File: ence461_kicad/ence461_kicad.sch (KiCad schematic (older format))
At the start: 54 parts, among them U1 LMV324, U2 LMV324, U3 LMV324, U4 74HC3G14DP, U5 LMV321, U6 NCV7344D13R2GOSCT-ND, U7 TPS717DRV-WSON, U8 TPS71433DRVR

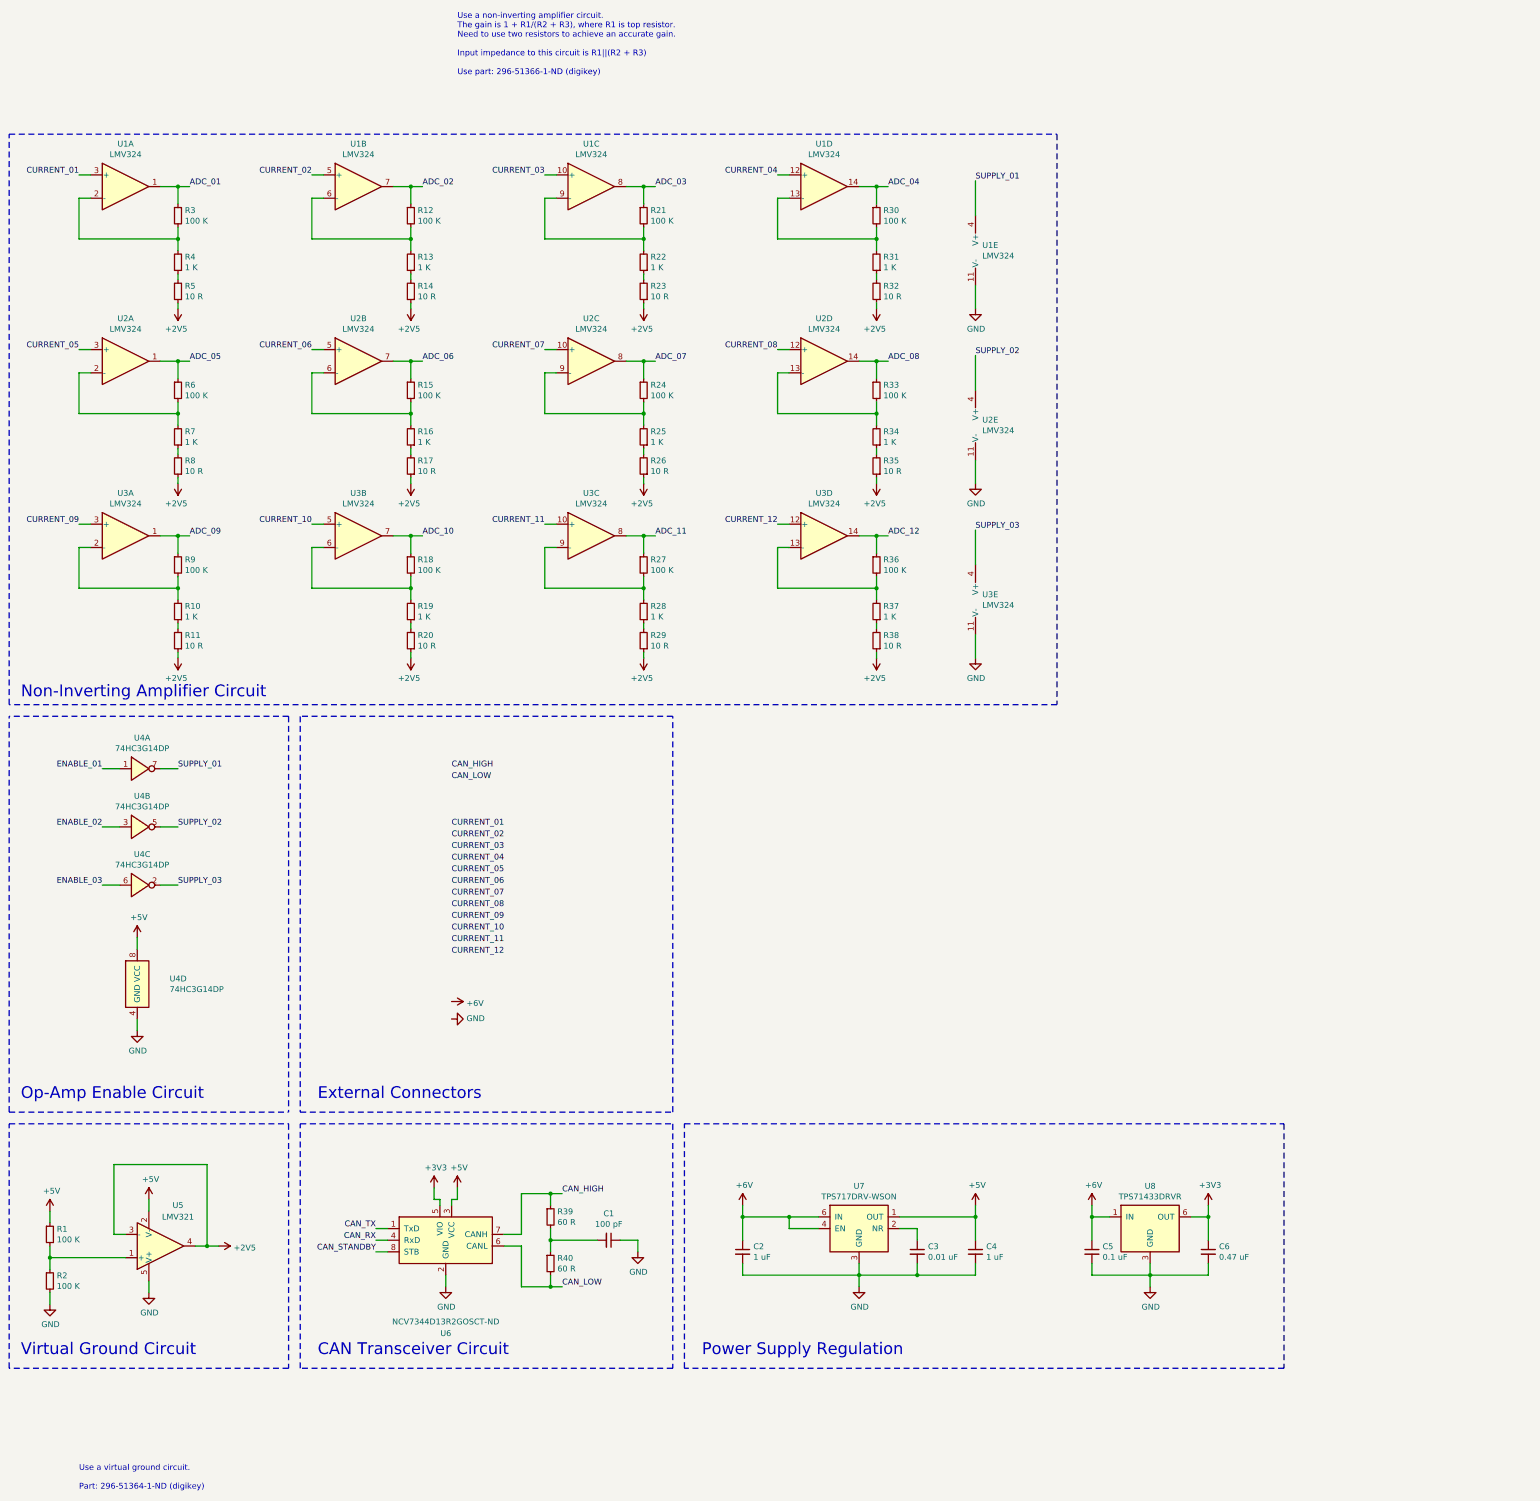
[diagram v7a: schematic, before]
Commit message: Added some stubs for micro gpio
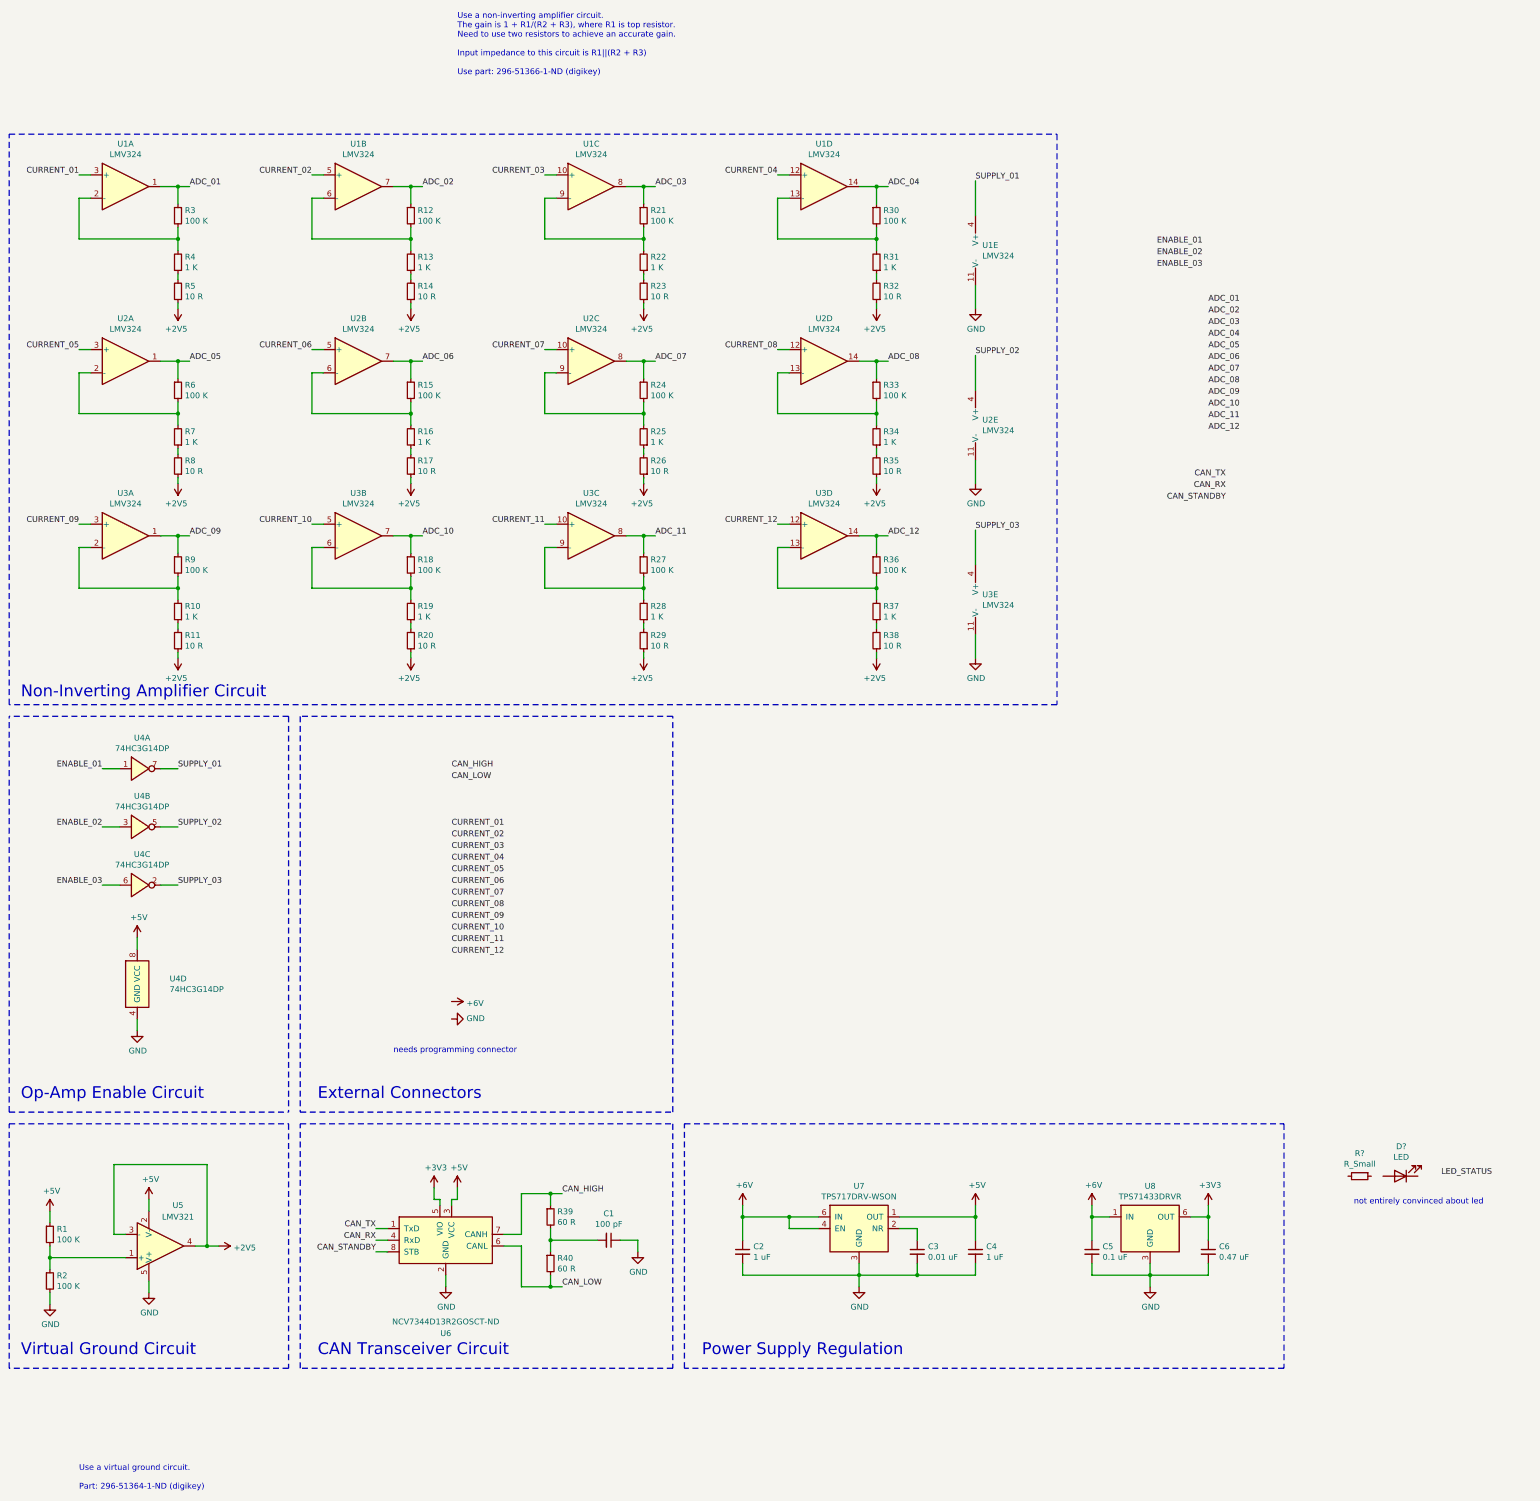
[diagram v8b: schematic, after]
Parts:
- added D?: LED, symbol Device:LED
- added R?: R_Small, symbol Device:R_Small
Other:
- note added: "needs programming connector"
- note added: "not entirely convinced about led"
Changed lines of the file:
@@
 Text Notes 3350 8850 0    101  ~ 0
 External Connectors
+Text Label 10950 1500 2    50   ~ 0
+ENABLE_01
+Text Label 10950 1700 2    50   ~ 0
+ENABLE_03
+Text Label 10950 1600 2    50   ~ 0
+ENABLE_02
+Text Label 11000 2000 0    50   ~ 0
+ADC_01
+Text Label 11000 2100 0    50   ~ 0
+ADC_02
+Text Label 11000 2200 0    50   ~ 0
+ADC_03
+Text Label 11000 2300 0    50   ~ 0
+ADC_04
+Text Label 11000 2400 0    50   ~ 0
+ADC_05
+Text Label 11000 2500 0    50   ~ 0
+ADC_06
+Text Label 11000 2600 0    50   ~ 0
+ADC_07
+Text Label 11000 2700 0    50   ~ 0
+ADC_08
+Text Label 11000 2800 0    50   ~ 0
+ADC_09
+Text Label 11000 2900 0    50   ~ 0
+ADC_10
+Text Label 11000 3000 0    50   ~ 0
+ADC_11
+Text Label 11000 3100 0    50   ~ 0
+ADC_12
+Text Label 11150 3700 2    50   ~ 0
+CAN_STANDBY
+Text Label 11150 3600 2    50   ~ 0
+CAN_RX
+Text Label 11150 3500 2    50   ~ 0
+CAN_TX
+$Comp
+L Device:LED D?
+U 1 1 5F290098
+P 12650 9500
+F 0 "D?" H 12643 9245 50  0000 C CNN
+F 1 "LED" H 12643 9336 50  0000 C CNN
+F 2 "" H 12650 9500 50  0001 C CNN
+F 3 "~" H 12650 9500 50  0001 C CNN
+	1    12650 9500
+	-1   0    0    1
+$EndComp
+Text Label 13000 9500 0    50   ~ 0
+LED_STATUS
+$Comp
+L Device:R_Small R?
+U 1 1 5F2AB002
+P 12300 9500
+F 0 "R?" V 12104 9500 50  0000 C CNN
+F 1 "R_Small" V 12195 9500 50  0000 C CNN
+F 2 "" H 12300 9500 50  0001 C CNN
+F 3 "~" H 12300 9500 50  0001 C CNN
+	1    12300 9500
+	0    1    1    0
+$EndComp
+Text Notes 12250 9750 0    50   ~ 0
+not entirely convinced about led
+Text Notes 4000 8450 0    50   ~ 0
+needs programming connector
 $EndSCHEMATC
